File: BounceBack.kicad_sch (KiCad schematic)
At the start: 0 parts

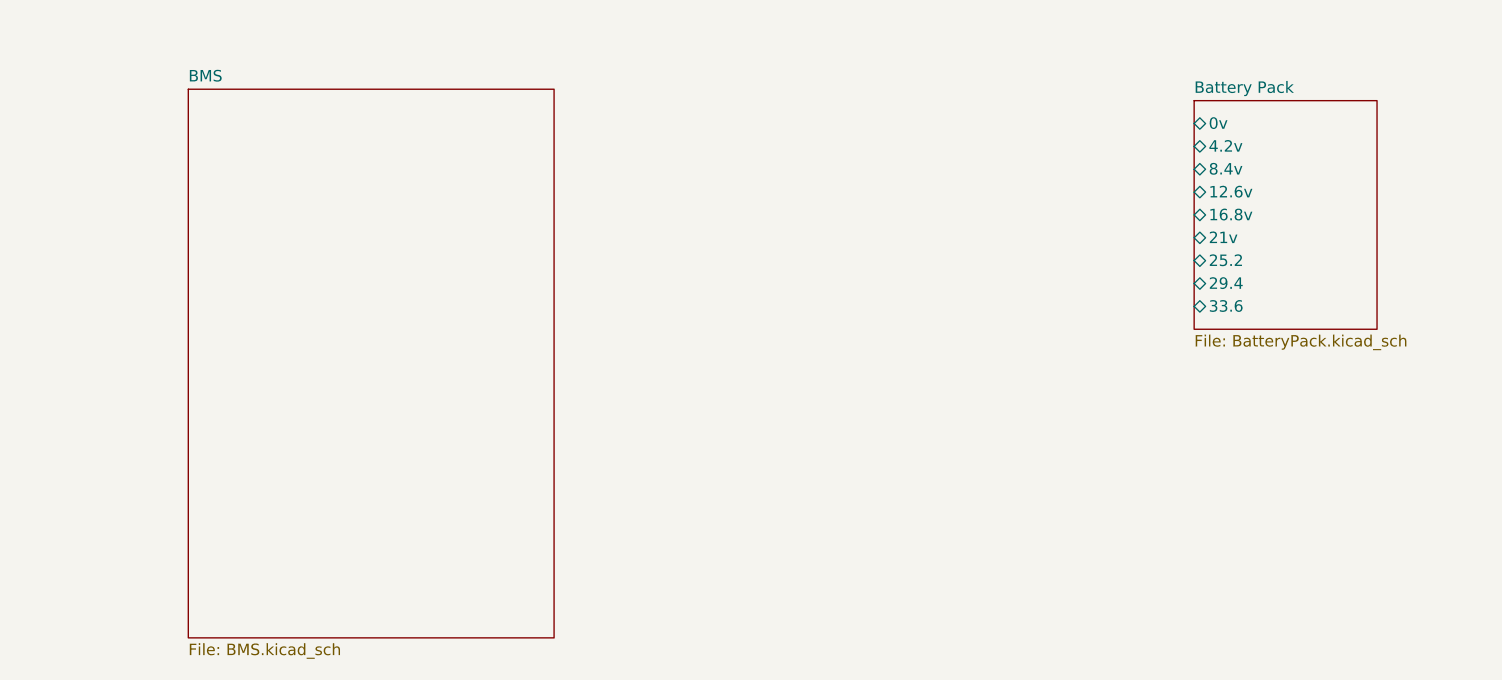
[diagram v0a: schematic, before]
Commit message: adds connectors and bom
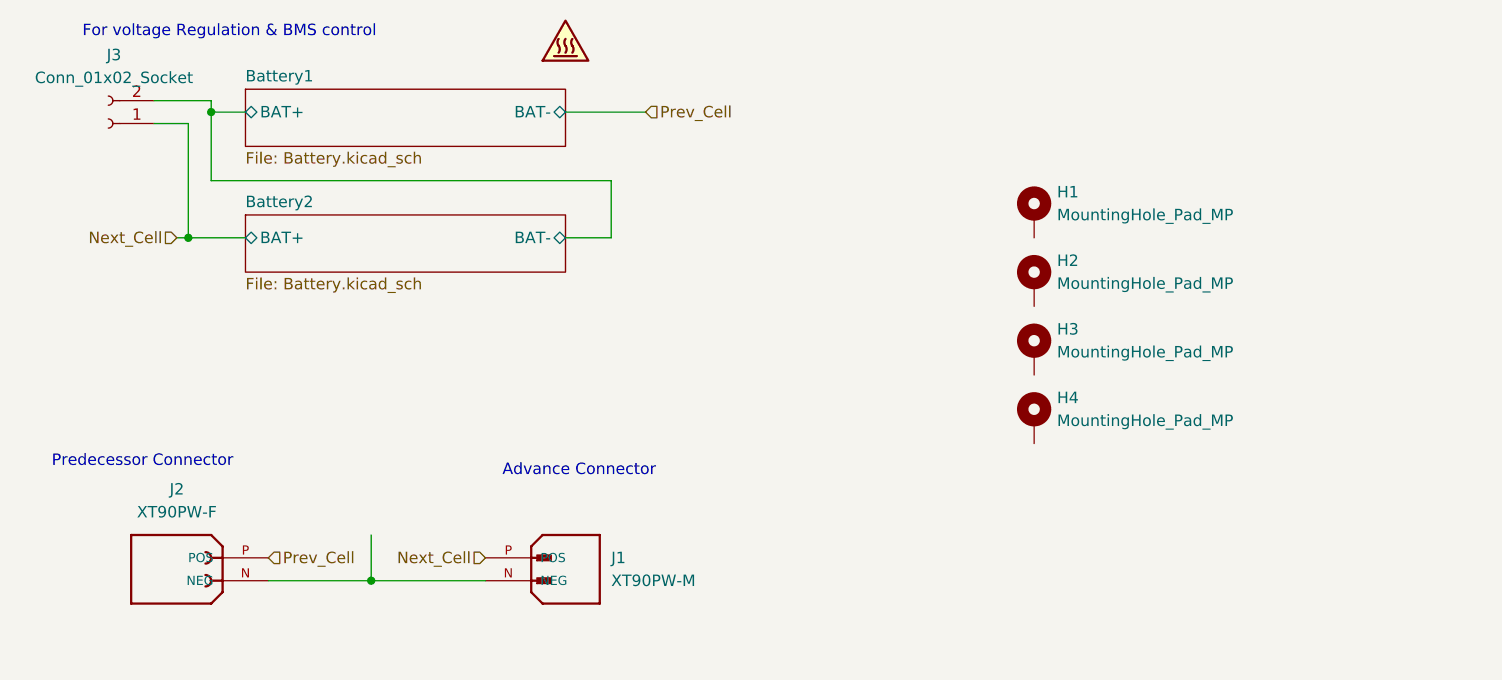
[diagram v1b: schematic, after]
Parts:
- added H1, H2, H3, H4: MountingHole_Pad_MP, MountingHole:MountingHole_4.3mm_M4_DIN965_Pad_TopBottom, symbol Mechanical:MountingHole_Pad_MP
- added J1: XT90PW-M, XT90PW-M:AMASS_XT90PW-M, symbol XT90PW-M:XT90PW-M
- added J2: XT90PW-F, XT90PW-F:AMASS_XT90PW-F, symbol XT90PW-F:XT90PW-F
- added J3: Conn_01x02_Socket, Connector_Molex:Molex_Mega-Fit_76829-0102_2x01_P5.70mm_Vertical, symbol Connector:Conn_01x02_Socket
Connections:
- new net: J1.N (NEG), J2.N (NEG)
- new net Battery1/BAT+: J3.2 (Pin_2)
- new net Next_Cell: J1.P (POS), J3.1 (Pin_1)
- new net Prev_Cell: J2.P (POS)
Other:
- removed sheet BMS
- removed sheet Battery Pack
- added sheet Battery1 (Battery.kicad_sch)
- added sheet Battery2 (Battery.kicad_sch)
- note added: "Advance Connector"
- note added: "For voltage Regulation & BMS control"
- note added: "Predecessor Connector"
